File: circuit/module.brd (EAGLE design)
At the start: 68.6 x 61 mm, 12 parts, among them IC1 4050

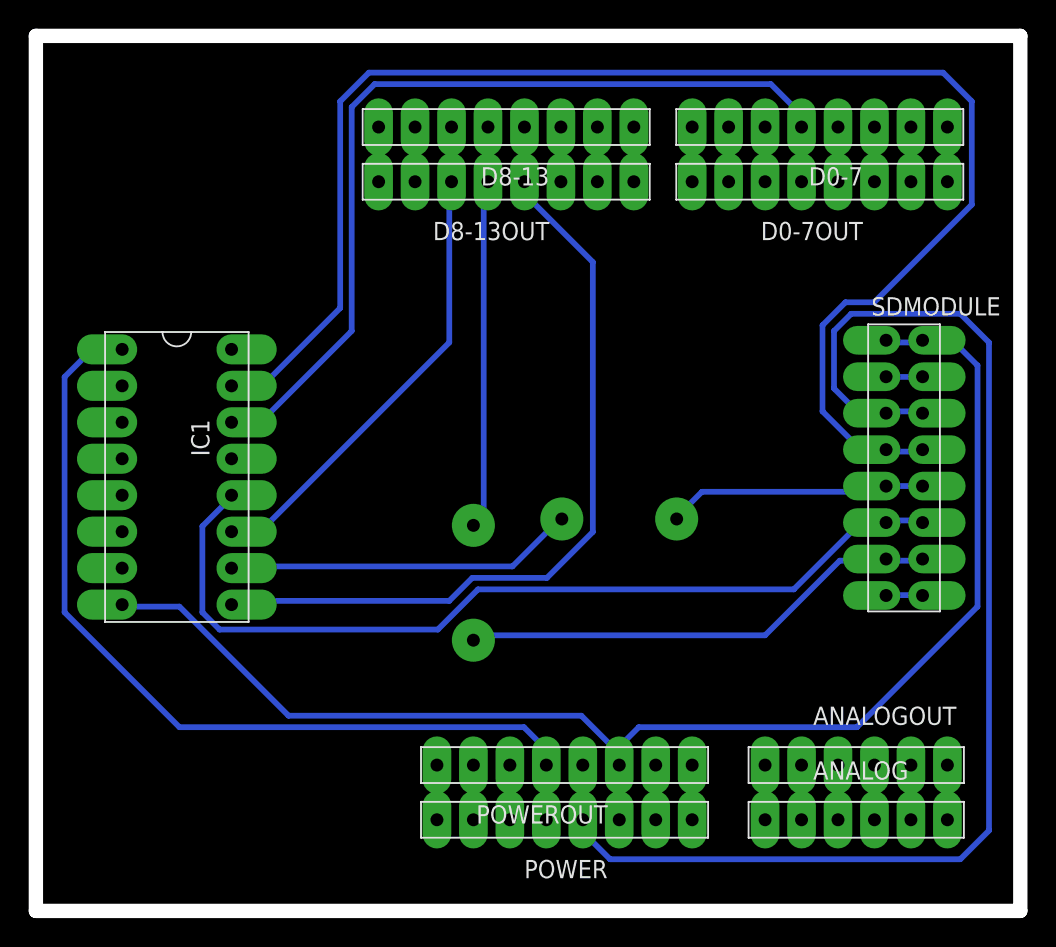
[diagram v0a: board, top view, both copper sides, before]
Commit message: Move 4050 to the right side of the SD module. Remove male-female pin couples, instead use a single group of pins.
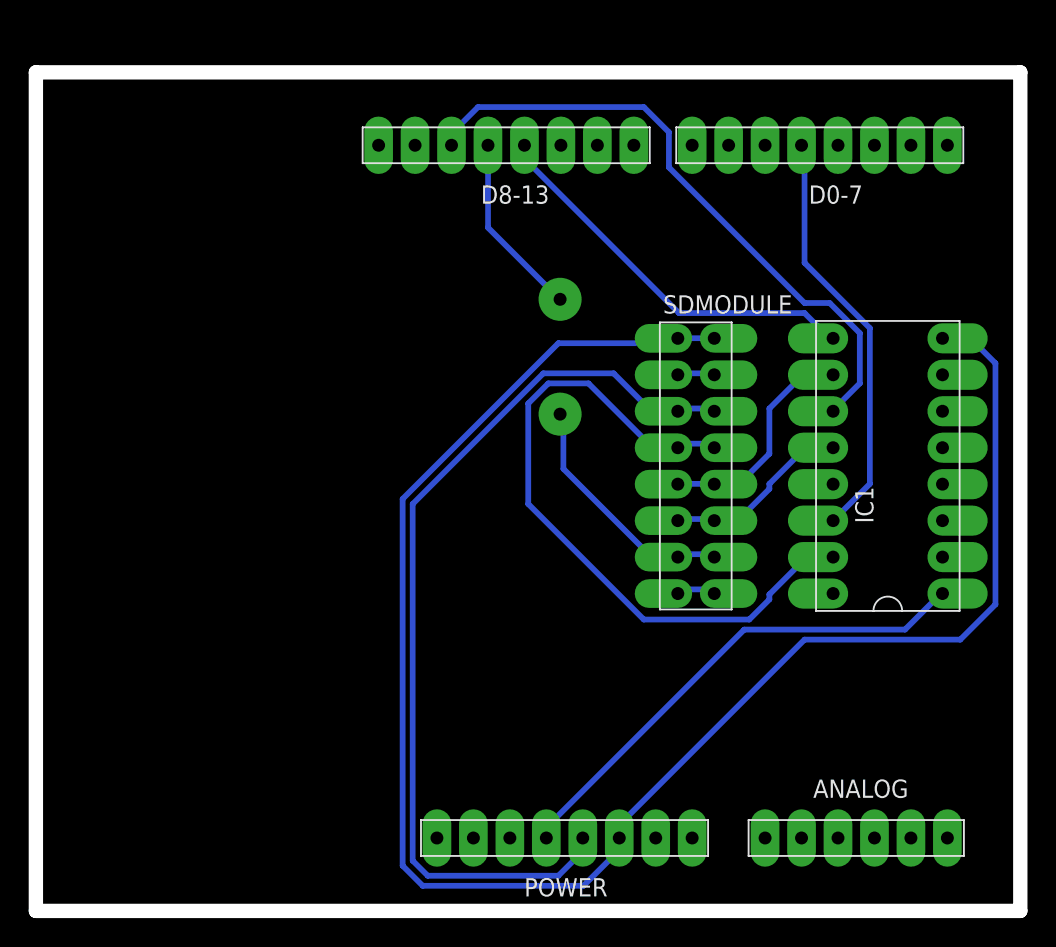
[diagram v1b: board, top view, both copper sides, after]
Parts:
- removed ANALOGOUT: PINPLUG6PINPLUG6, simple-parts:PINPLUG6
- removed D0-7OUT, D8-13OUT, POWEROUT: PINPLUG8PINPLUG8, simple-parts:PINPLUG8
- removed U$2: SHORTSHORT5, simple-parts:SHORT5
- moved IC1 49.5 mm to (59.4, 31.0), turned to 90 degrees
- moved U$1 16.9 mm to (36.5, 38.6)
- moved SDMODULE 14.5 mm to (46.0, 31.0)
- moved ANALOG 1.27 mm to (57.1, 5.08)
- moved POWER 1.27 mm to (36.8, 5.08)
- moved D0-7 1.27 mm to (54.6, 53.3)
- moved D8-13 1.27 mm to (32.8, 53.3)
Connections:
- removed net N$10: D8-13.P$7, D8-13OUT.P$7
- removed net N$14: D8-13.P$3, D8-13OUT.P$3
- removed net N$15: D8-13.P$2, D8-13OUT.P$2
- removed net N$16: D8-13.P$1, D8-13OUT.P$1
- removed net N$17: POWER.P$1, POWEROUT.P$1
- removed net N$18: POWER.P$2, POWEROUT.P$2
- removed net N$2: D0-7.P$7, D0-7OUT.P$7
- removed net N$21: IC1.P$10, U$2.P$2
- removed net N$23: POWER.P$6, POWEROUT.P$6
- removed net N$24: POWER.P$7, POWEROUT.P$7
- removed net N$25: POWER.P$8, POWEROUT.P$8
- removed net N$26: ANALOG.P$1, ANALOGOUT.P$1
- removed net N$27: ANALOG.P$2, ANALOGOUT.P$2
- removed net N$28: ANALOG.P$3, ANALOGOUT.P$3
- removed net N$29: ANALOG.P$4, ANALOGOUT.P$4
- removed net N$3: D0-7.P$6, D0-7OUT.P$6
- removed net N$30: ANALOG.P$5, ANALOGOUT.P$5
- removed net N$31: ANALOG.P$6, ANALOGOUT.P$6
- removed net N$40: IC1.P$1, POWER.P$5, POWEROUT.P$5
- removed net N$5: D0-7.P$4, D0-7OUT.P$4
- removed net N$6: D0-7.P$3, D0-7OUT.P$3
- removed net N$7: D0-7.P$2, D0-7OUT.P$2
- removed net N$8: D0-7.P$1, D0-7OUT.P$1
- removed net N$9: D8-13.P$8, D8-13OUT.P$8
- net N$1: now also IC1.P$1, POWER.P$5; no longer D0-7.P$8, D0-7OUT.P$8
- net N$13: no longer D8-13OUT.P$4
- net N$20: no longer POWEROUT.P$3
- net N$22: no longer D8-13OUT.P$5
- net N$33: now also IC1.P$10; no longer U$2.P$1
- net N$34: no longer D8-13OUT.P$6
- net N$39: no longer POWEROUT.P$4
- net N$4: no longer D0-7OUT.P$5
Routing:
- net N$40: track 63.9 -> 0.00 mm
- net N$32: track 105.2 -> 49.4 mm
- net N$11: track 62.9 -> 13.2 mm
- net N$4: track 64.3 -> 29.2 mm
- net N$1: track 3.96 -> 35.1 mm
- net N$13: track 57.7 -> 27.7 mm
- net N$39: track 91.8 -> 65.0 mm
- net N$20: track 98.1 -> 124.3 mm
- net N$21: track 24.4 -> 0.00 mm
- net N$12: track 33.7 -> 17.3 mm
- net N$22: track 28.5 -> 12.8 mm
- net N$34: track 35.8 -> 44.2 mm
- net N$14: track 4.05 -> 0.00 mm
- net N$23: track 4.03 -> 0.00 mm
- net N$7: track 4.02 -> 0.00 mm
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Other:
- board size 68.6 x 61 mm -> 68.6 x 58.4 mm

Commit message: Update schematic and the board. Upload latest version build pictures. Update README accordingly.
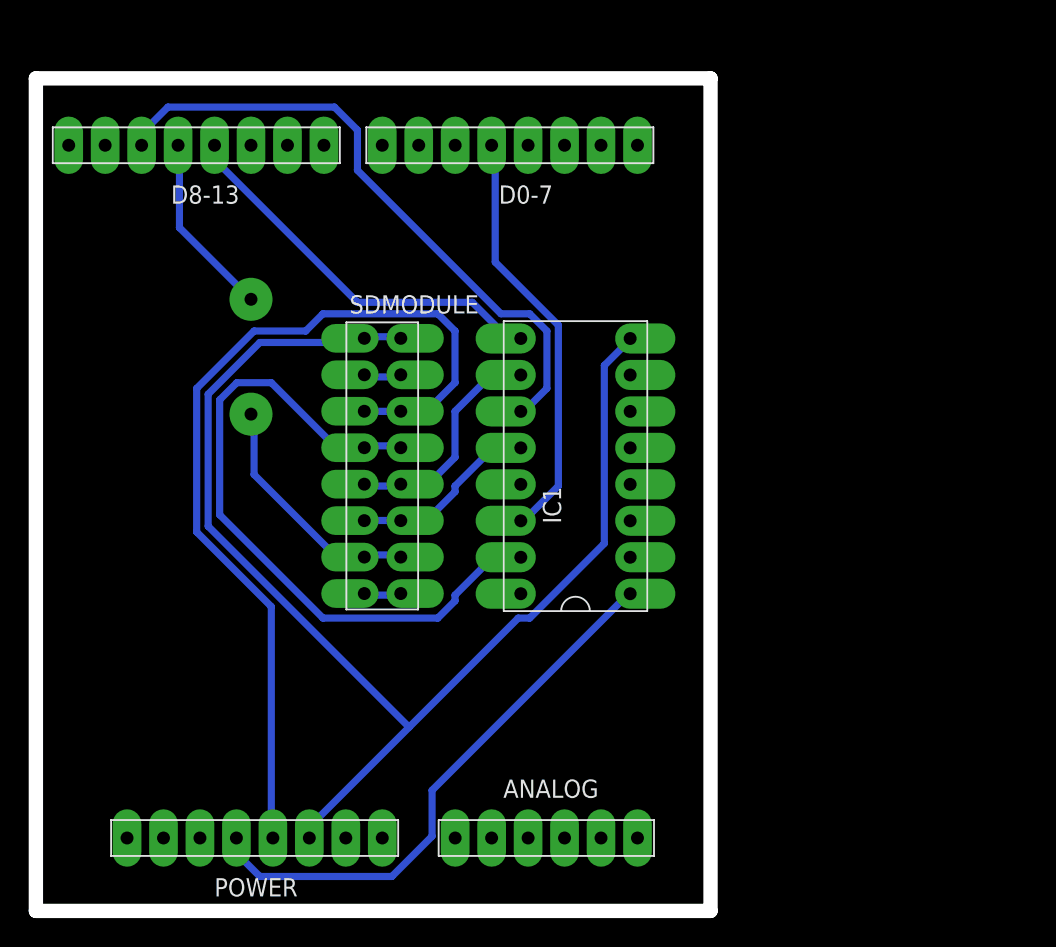
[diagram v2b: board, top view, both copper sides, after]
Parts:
- moved SDMODULE 21.8 mm to (24.1, 31.0)
- moved IC1 21.8 mm to (37.6, 31.0)
- moved ANALOG 21.6 mm to (35.6, 5.08)
- moved D0-7 21.6 mm to (33.0, 53.3)
- moved D8-13 21.6 mm to (11.2, 53.3)
- moved POWER 21.6 mm to (15.2, 5.08)
- moved U$1 21.5 mm to (15.0, 38.6)
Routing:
- net N$20: track 124.3 -> 88.7 mm
- net N$1: track 35.1 -> 39.2 mm
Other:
- board size 68.6 x 58.4 mm -> 47 x 58.4 mm
